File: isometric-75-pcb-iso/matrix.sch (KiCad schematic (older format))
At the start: 252 parts, among them SW201 Rotary_Encoder_Switch

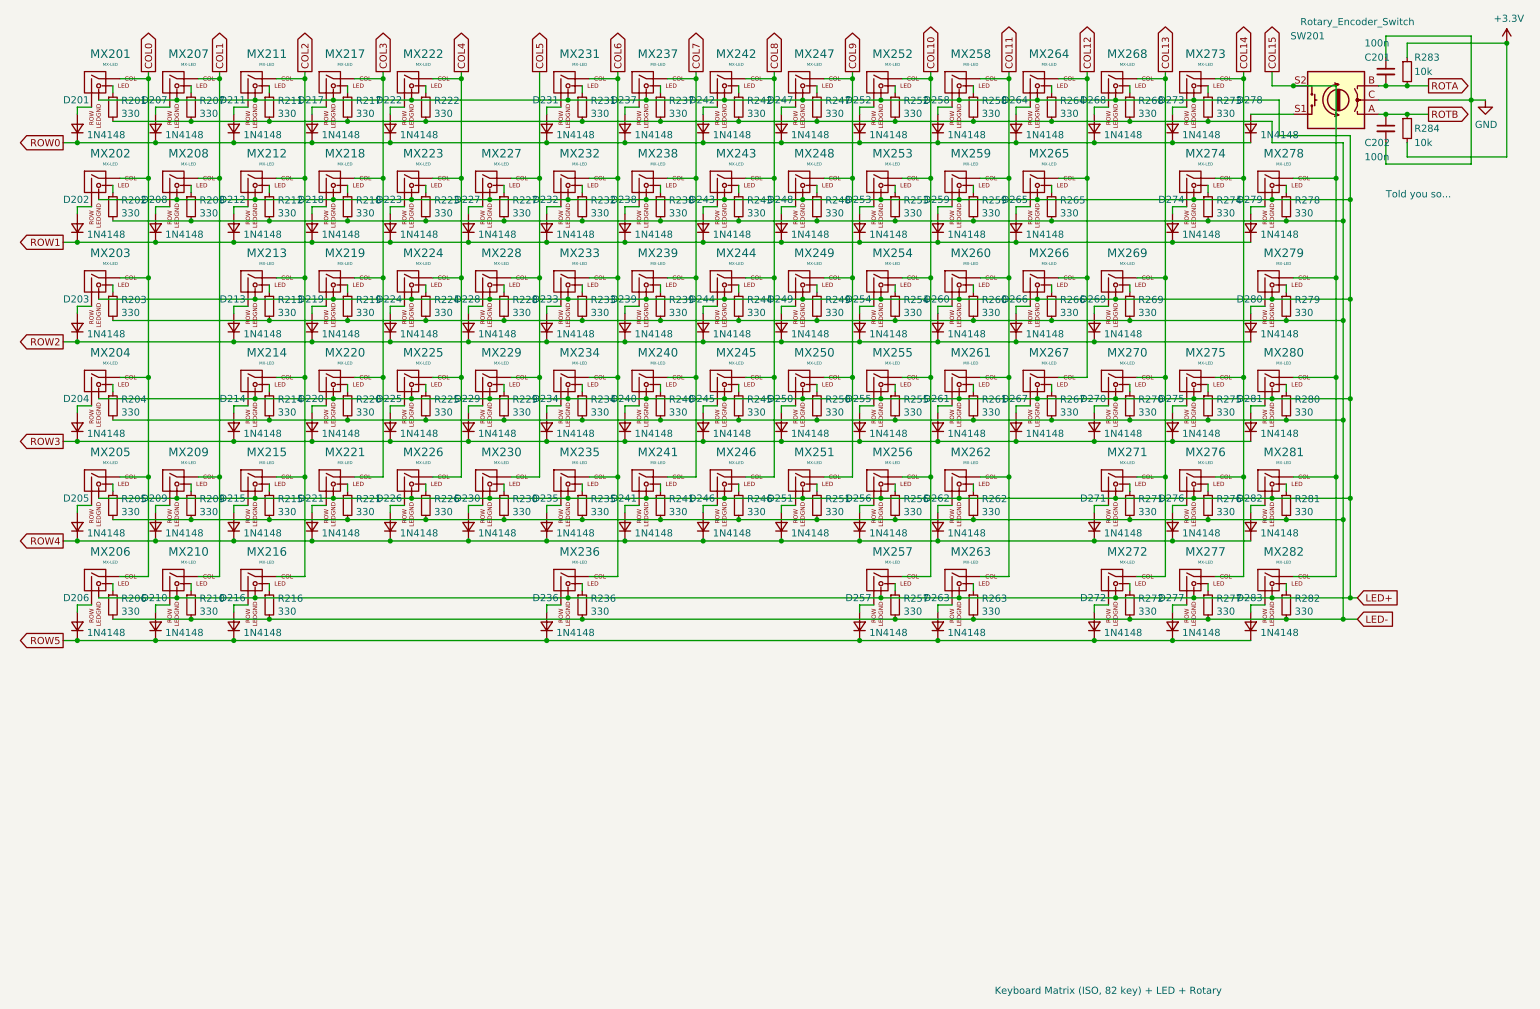
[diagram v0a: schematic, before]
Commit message: added ground planes, various minor fixes
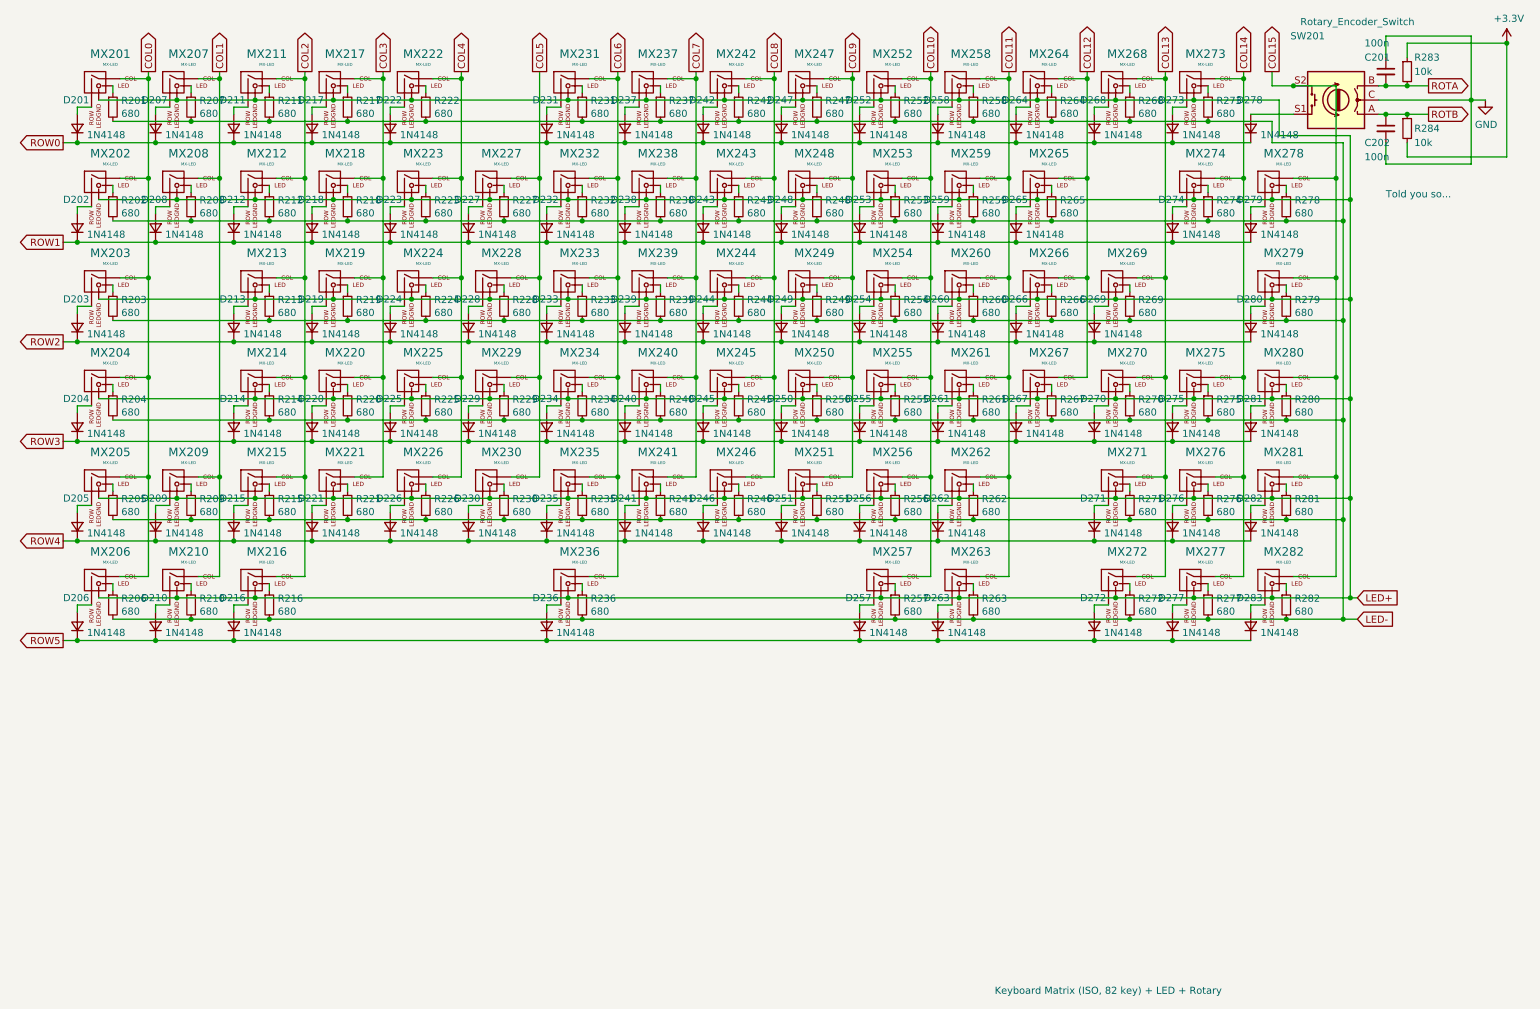
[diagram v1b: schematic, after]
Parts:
- R201, R202, R203, R204, R205, R206, R207, R208, R209, R210, R211, R212, R213, R214, R215, R216, R217, R218, R219, R220, R221, R222, R223, R224, R225, R226, R227, R228, R229, R230, R231, R232, R233, R234, R235, R236, R237, R238, R239, R240, R241, R242, R243, R244, R245, R246, R247, R248, R249, R250, R251, R252, R253, R254, R255, R256, R257, R258, R259, R260, R261, R262, R263, R264, R265, R266, R267, R268, R269, R270, R271, R272, R273, R274, R275, R276, R277, R278, R279, R280, R281, R282: value 330 -> 680

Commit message: minor layout fixes (thanks gLu3xb3rchi)
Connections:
- net LED+ renamed +5V
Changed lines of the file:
@@
 	9350 1000 9350 1100
 Text GLabel 9950 4700 2    50   Input ~ 0
-LED+
++5V
 Text GLabel 9950 4850 2    50   Input ~ 0
 LED-
